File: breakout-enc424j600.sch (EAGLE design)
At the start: 25 parts, among them IC1 ENC424J600-I/PT, J1 HRJACK-HR911105A

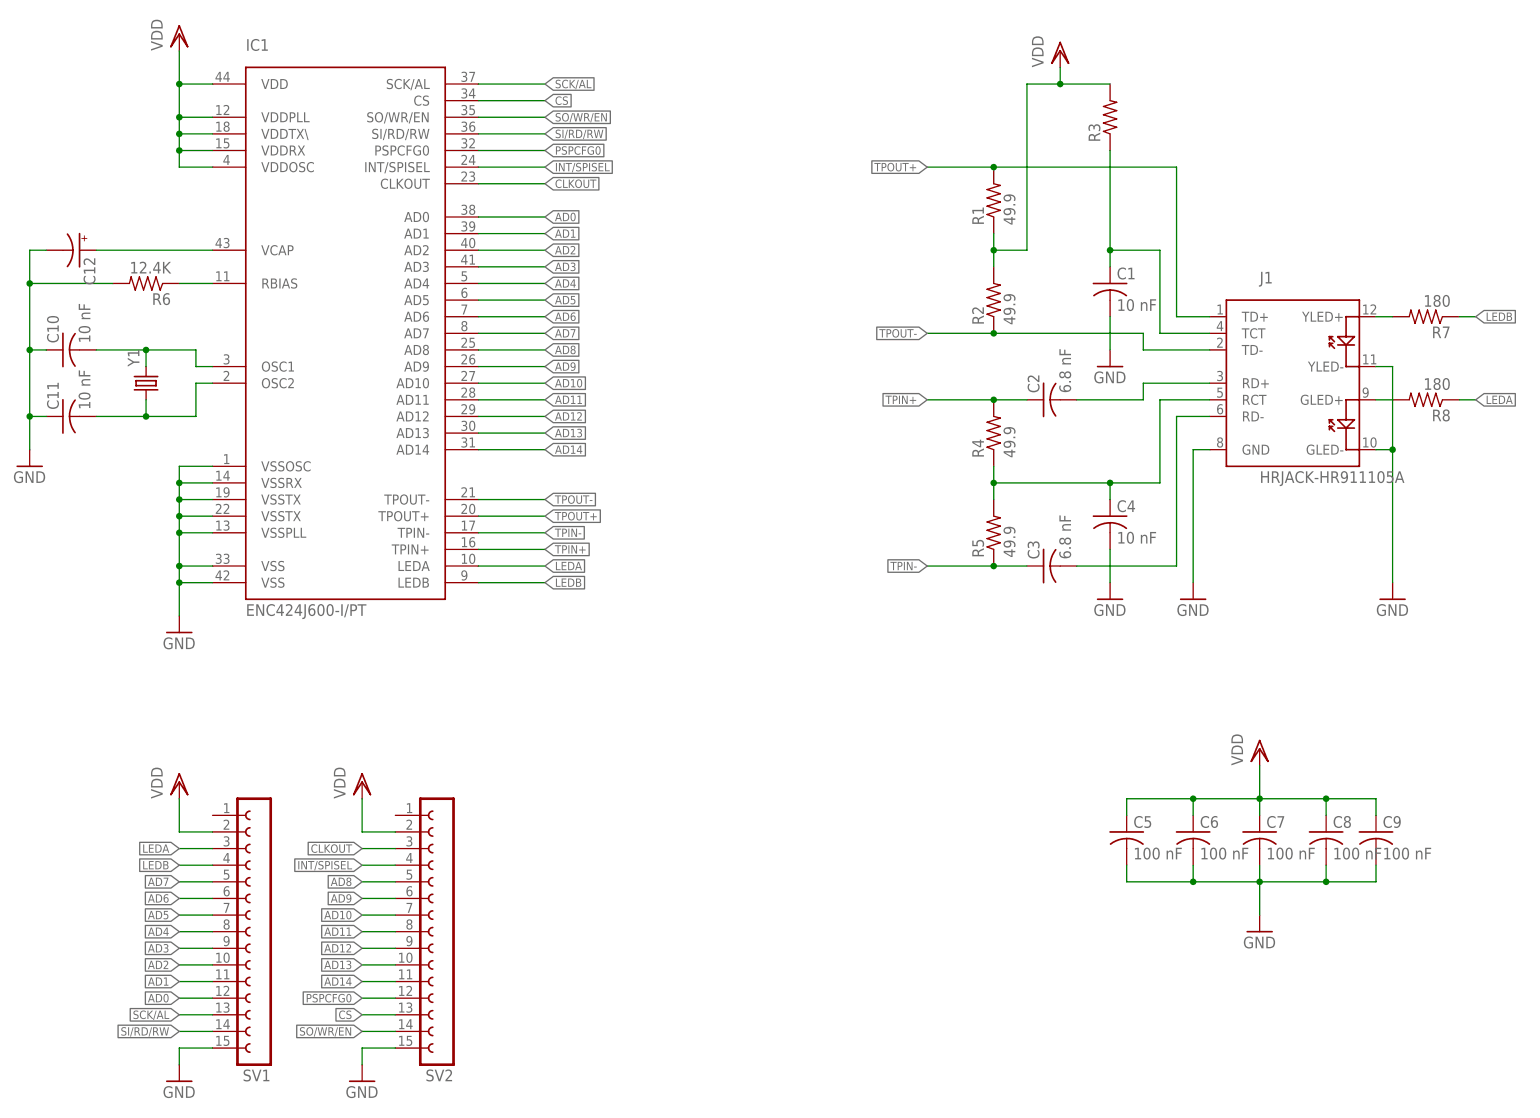
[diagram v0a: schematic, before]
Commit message: Add pinout on silkscreen, change pin headers, connect ground shield on ethernet, modified board dimension
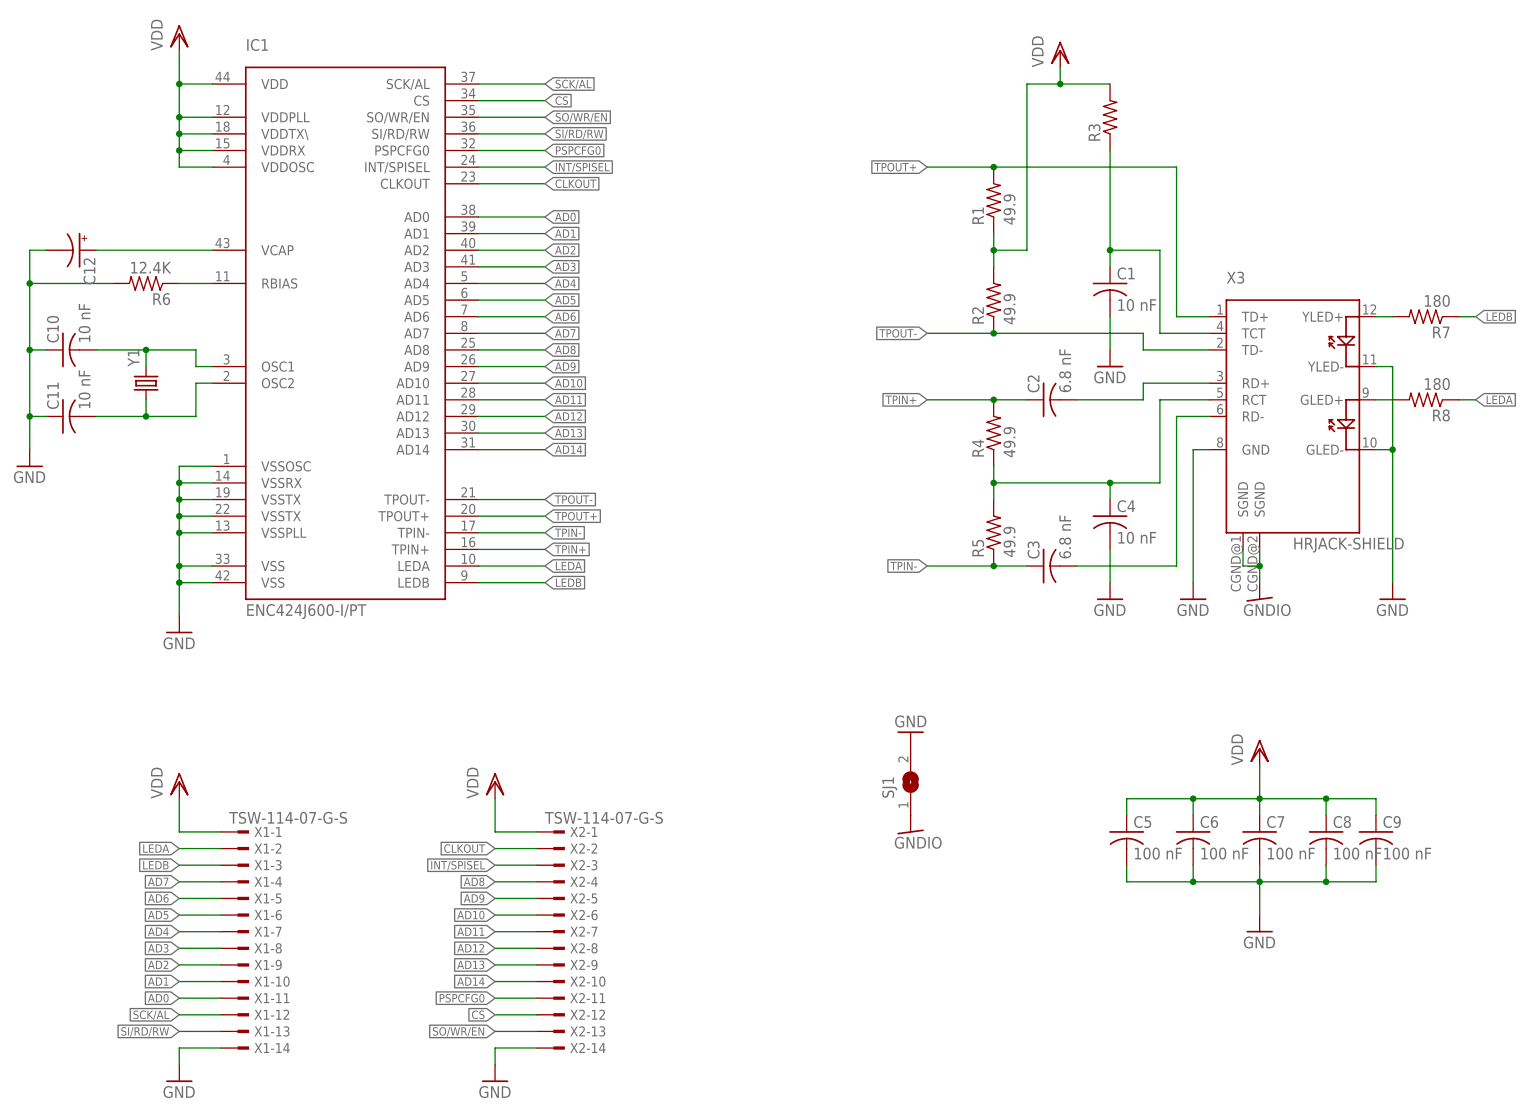
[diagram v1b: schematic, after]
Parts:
- removed J1: HRJACK-HR911105A, various-electromechanical:HRJACK-HR911105A
- removed SV1, SV2: (no value), con-lsta:FE15-1
- added SJ1: (no value), jumper:SJW
- added X1, X2: TSW-114-07-G-S, con-samtec:TSW-114-07-G-S
- added X3: HRJACK-SHIELD, various-electromechanical:HRJACK-SHIELD
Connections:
- new net GNDIO: SJ1.1, X3.SGND@1, X3.SGND@2
- net AD0: now also X1-11.1; no longer SV1.12
- net AD1: now also X1-10.1; no longer SV1.11
- net AD10: now also X2-6.1; no longer SV2.7
- net AD11: now also X2-7.1; no longer SV2.8
- net AD12: now also X2-8.1; no longer SV2.9
- net AD13: now also X2-9.1; no longer SV2.10
- net AD14: now also X2-10.1; no longer SV2.11
- net AD2: now also X1-9.1; no longer SV1.10
- net AD3: now also X1-8.1; no longer SV1.9
- net AD4: now also X1-7.1; no longer SV1.8
- net AD5: now also X1-6.1; no longer SV1.7
- net AD6: now also X1-5.1; no longer SV1.6
- net AD7: now also X1-4.1; no longer SV1.5
- net AD8: now also X2-4.1; no longer SV2.5
- net AD9: now also X2-5.1; no longer SV2.6
- net CLKOUT: now also X2-2.1; no longer SV2.3
- net CS: now also X2-12.1; no longer SV2.13
- net GND: now also SJ1.2, X1-14.1, X2-14.1, X3.GLED-, X3.GND, X3.YLED-; no longer J1.GLED-, J1.GND, J1.YLED-, SV1.15, SV2.15
- net INT/SPISEL: now also X2-3.1; no longer SV2.4
- net LEDA: now also X1-2.1; no longer SV1.3
- net LEDB: now also X1-3.1; no longer SV1.4
- net N$2: now also X3.TCT; no longer J1.TCT
- net N$4: now also X3.RD+; no longer J1.RD+
- net N$5: now also X3.RD-; no longer J1.RD-
- net N$6: now also X3.RCT; no longer J1.RCT
- net N$8: now also X3.GLED+; no longer J1.GLED+
- net N$9: now also X3.YLED+; no longer J1.YLED+
- net PSPCFG0: now also X2-11.1; no longer SV2.12
- net SCK/AL: now also X1-12.1; no longer SV1.13
- net SI/RD/RW: now also X1-13.1; no longer SV1.14
- net SO/WR/EN: now also X2-13.1; no longer SV2.14
- net TPOUT+: now also X3.TD+; no longer J1.TD+
- net TPOUT-: now also X3.TD-; no longer J1.TD-
- net VDD: now also X1-1.1, X2-1.1; no longer SV1.2, SV2.2

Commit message: Add missing component values
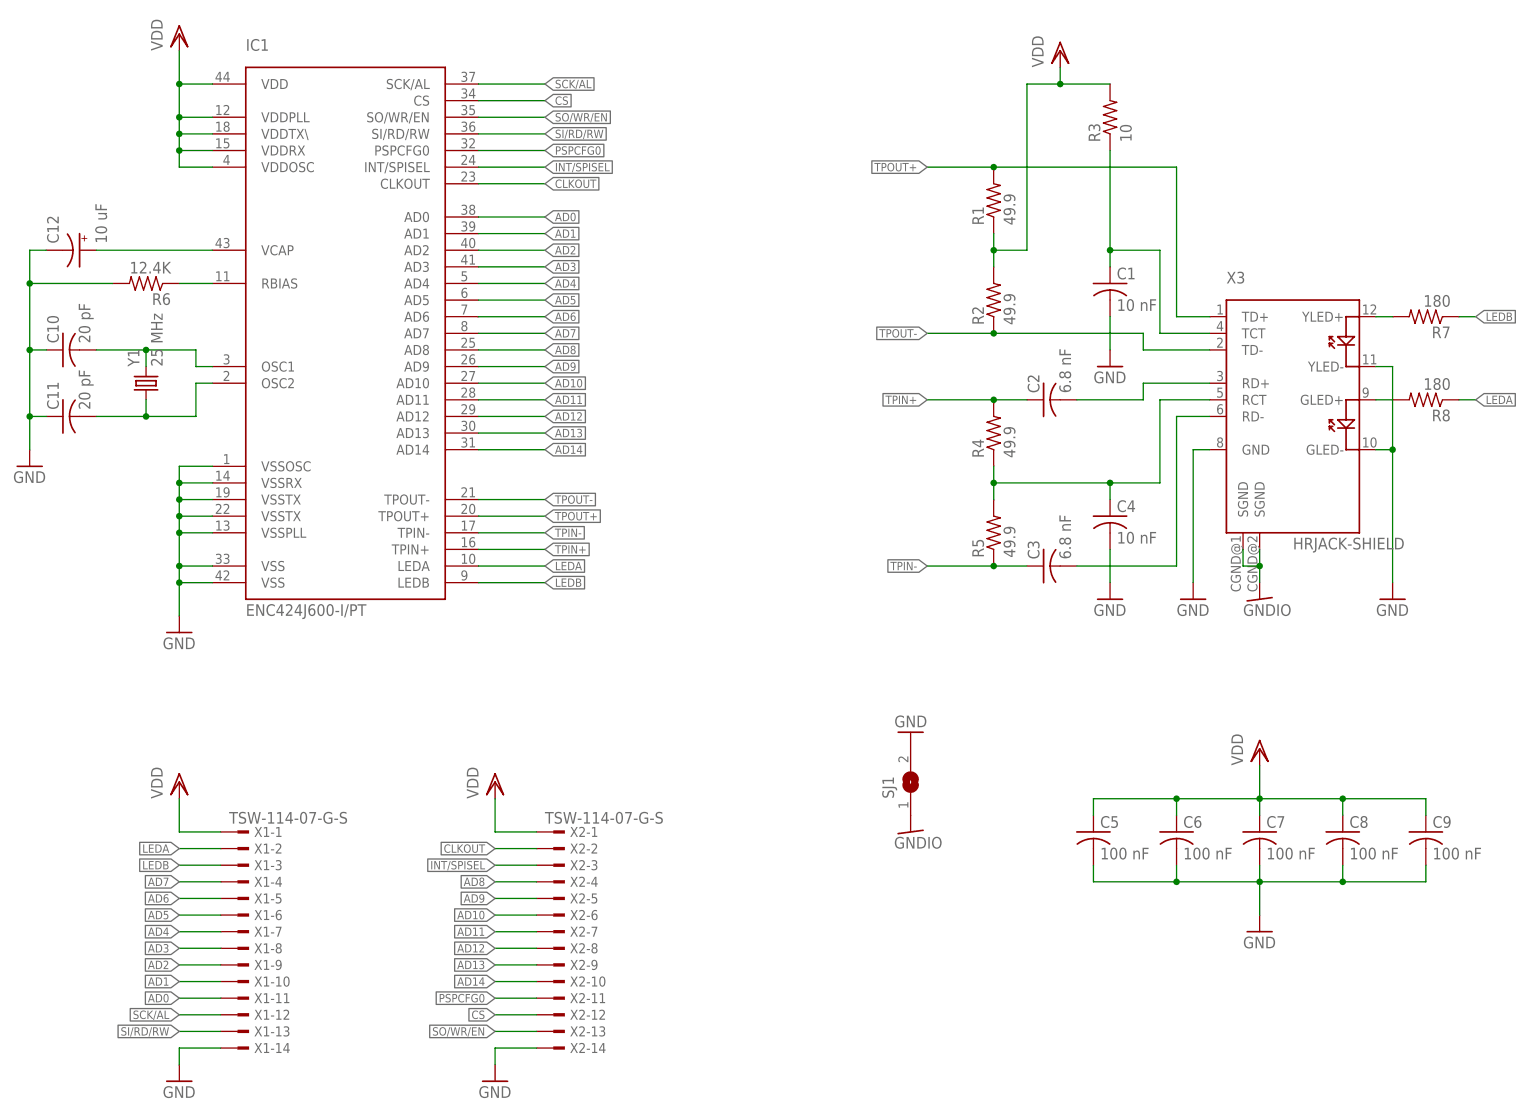
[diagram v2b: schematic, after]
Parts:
- C10, C11: value 10 nF -> 20 pF
- C12: value (none) -> 10 uF
- R3: value (none) -> 10
- Y1: value (none) -> 25 MHz
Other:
- moved on the sheet: C5, C6, C8, C9
